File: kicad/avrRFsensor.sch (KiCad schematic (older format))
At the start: 13 parts, among them U1 ATTINY85-20SU, X1 18MHz HC49USSMD

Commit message: schematics on atmega168 tqfp32
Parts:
- removed U1: ATTINY85-20SU, SO8-200, symbol ATTINY85-S
- added D3: 3V6, symbol ZENER
- added R5: 25, symbol R
- added R6, R7, R8: 10k, symbol R
- added U1: ATMEGA168PA-A, TQFP32, symbol ATMEGA168PA-A
- added U2: RFM69, ~, symbol RFM69
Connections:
- net labels added: MISO_RFM, MISO_USB, MOSI_RFM, SCK_RFM, SCK_USB, VCC +5
- wire segments 36 -> 56
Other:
- moved on the sheet: C3
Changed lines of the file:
@@
 LIBS:contrib
 LIBS:valves
+LIBS:rfm69
 LIBS:avrRFsensor-cache
 EELAYER 27 0
@@
 Connection ~ 1500 2150
 Wire Wire Line
-	3400 2750 3850 2750
-Wire Wire Line
 	1500 1350 1500 1450
-Connection ~ 6700 3250
-Wire Wire Line
-	3400 2850 3850 2850
+Connection ~ 1050 7300
 Wire Wire Line
 	950  4650 1100 4650
@@
 L GND #PWR01
 U 1 1 4E041C8A
-P 6700 3300
-F 0 "#PWR01" H 6700 3300 30  0001 C CNN
-F 1 "GND" H 6700 3230 30  0001 C CNN
-F 2 "" H 6700 3300 60  0001 C CNN
-F 3 "" H 6700 3300 60  0001 C CNN
-	1    6700 3300
+P 1050 7350
+F 0 "#PWR01" H 1050 7350 30  0001 C CNN
+F 1 "GND" H 1050 7280 30  0001 C CNN
+F 2 "" H 1050 7350 60  0001 C CNN
+F 3 "" H 1050 7350 60  0001 C CNN
+	1    1050 7350
 	1    0    0    -1
 $EndComp
@@
 	1    1350 1000
 	0    1    1    0
-$EndComp
-$Comp
-L ATTINY85-S U1
-U 1 1 4E03B504
-P 5200 3000
-F 0 "U1" H 5300 3050 60  0000 C CNN
-F 1 "ATTINY85-20SU" H 5700 2750 60  0000 C CNN
-F 2 "SO8-200" H 5450 2250 60  0001 C CNN
-F 3 "" H 5200 3000 60  0001 C CNN
-	1    5200 3000
-	1    0    0    -1
 $EndComp
 $Comp
@@
 L CP1 C3
 U 1 1 4B61D8DC
-P 6700 3000
-F 0 "C3" H 6750 3100 50  0000 L CNN
-F 1 "4.7uF" H 6750 2900 50  0000 L CNN
-F 2 "" H 6700 3000 60  0001 C CNN
-F 3 "" H 6700 3000 60  0001 C CNN
-	1    6700 3000
+P 1050 7050
+F 0 "C3" H 1100 7150 50  0000 L CNN
+F 1 "4.7uF" H 1100 6950 50  0000 L CNN
+F 2 "" H 1050 7050 60  0001 C CNN
+F 3 "" H 1050 7050 60  0001 C CNN
+	1    1050 7050
 	1    0    0    -1
 $EndComp
@@
 	1    0    0    -1
 $EndComp
-Text GLabel 6900 2750 2    60   Input ~ 0
+Text GLabel 1250 6800 2    60   Input ~ 0
 VCC
 Text GLabel 1600 4350 2    60   Input ~ 0
@@
 Wire Wire Line
 	1000 1000 1100 1000
-Text GLabel 6900 3250 2    60   Input ~ 0
+Text GLabel 1250 7300 2    60   Input ~ 0
 GND
 Text GLabel 900  1350 0    60   Input ~ 0
@@
 Wire Wire Line
 	900  1350 1000 1350
-Text GLabel 3400 3050 0    60   Input ~ 0
+Text GLabel 5500 2900 2    60   Input ~ 0
 XTAL1
-Text GLabel 3400 3150 0    60   Input ~ 0
+Text GLabel 5500 3000 2    60   Input ~ 0
 XTAL2
-Wire Wire Line
-	3400 3050 3850 3050
-Wire Wire Line
-	3850 3150 3400 3150
 Text GLabel 950  5000 0    60   Input ~ 0
 GND
-Text GLabel 3400 3250 0    60   Input ~ 0
+Text GLabel 5500 3750 2    60   Input ~ 0
 RESET
-Wire Wire Line
-	3850 3250 3400 3250
 Text GLabel 1300 2900 2    60   Input ~ 0
 MOSI
 Wire Wire Line
 	1300 2900 1150 2900
-Text GLabel 3400 2750 0    60   Input ~ 0
+Text GLabel 5500 2600 2    60   Input ~ 0
 MOSI
 Wire Wire Line
-	6700 3200 6700 3300
-Wire Wire Line
-	6700 2700 6700 2800
-Connection ~ 6700 2750
+	1050 7250 1050 7350
+Wire Wire Line
+	1050 6750 1050 6850
+Connection ~ 1050 6800
 $Comp
 L VCC #PWR02
 U 1 1 54B791F6
-P 6700 2700
-F 0 "#PWR02" H 6700 2800 30  0001 C CNN
-F 1 "VCC" H 6700 2800 30  0000 C CNN
-F 2 "" H 6700 2700 60  0000 C CNN
-F 3 "" H 6700 2700 60  0000 C CNN
-	1    6700 2700
-	1    0    0    -1
-$EndComp
-Wire Wire Line
-	6550 3250 6900 3250
-Wire Wire Line
-	6550 2750 6900 2750
+P 1050 6750
+F 0 "#PWR02" H 1050 6850 30  0001 C CNN
+F 1 "VCC" H 1050 6850 30  0000 C CNN
+F 2 "" H 1050 6750 60  0000 C CNN
+F 3 "" H 1050 6750 60  0000 C CNN
+	1    1050 6750
+	1    0    0    -1
+$EndComp
 Text GLabel 1300 2800 2    60   Input ~ 0
 MISO
 Wire Wire Line
 	1300 2800 1150 2800
-Text GLabel 3400 2850 0    60   Input ~ 0
+Text GLabel 5500 2700 2    60   Input ~ 0
 MISO
 Text GLabel 1600 4100 2    60   Input ~ 0
-MISO
+MISO_USB
 Wire Wire Line
 	1500 4100 1600 4100
@@
 Wire Wire Line
 	1300 2700 1150 2700
-Text GLabel 3400 2950 0    60   Input ~ 0
+Text GLabel 5500 2800 2    60   Input ~ 0
 SCK
-Wire Wire Line
-	3850 2950 3400 2950
 Text GLabel 1600 3850 2    60   Input ~ 0
-SCK
+SCK_USB
 Wire Wire Line
 	1500 3850 1600 3850
 Text GLabel 1450 5600 2    60   Input ~ 0
-VCC
+VCC +5
 Text GLabel 1450 5300 2    60   Input ~ 0
 GND
@@
 Wire Wire Line
 	1000 4350 900  4350
+$Comp
+L ATMEGA168PA-A U1
+U 1 1 54B7A49D
+P 4300 3400
+F 0 "U1" H 3550 4650 40  0000 L BNN
+F 1 "ATMEGA168PA-A" H 4700 2000 40  0000 L BNN
+F 2 "TQFP32" H 4300 3400 30  0000 C CIN
+F 3 "" H 4300 3400 60  0000 C CNN
+	1    4300 3400
+	1    0    0    -1
+$EndComp
+Wire Wire Line
+	5300 3750 5500 3750
+Wire Wire Line
+	5500 3000 5300 3000
+Wire Wire Line
+	5500 2900 5300 2900
+Wire Wire Line
+	1250 7300 1050 7300
+Wire Wire Line
+	1250 6800 1050 6800
+Text GLabel 3200 4600 0    60   Input ~ 0
+GND
+Text GLabel 3200 2300 0    60   Input ~ 0
+VCC
+Text GLabel 3200 2400 0    60   Input ~ 0
+VCC
+Wire Wire Line
+	3400 2300 3200 2300
+Wire Wire Line
+	3200 2400 3400 2400
+Text GLabel 3200 2600 0    60   Input ~ 0
+VCC
+Wire Wire Line
+	3400 2600 3200 2600
+Wire Wire Line
+	5500 2700 5300 2700
+Wire Wire Line
+	5500 2800 5300 2800
+Wire Wire Line
+	5500 2600 5300 2600
+Wire Wire Line
+	3400 4600 3200 4600
+Text GLabel 3200 4500 0    60   Input ~ 0
+GND
+Text GLabel 3200 4400 0    60   Input ~ 0
+GND
+Wire Wire Line
+	3200 4400 3400 4400
+Wire Wire Line
+	3400 4500 3200 4500
+$Comp
+L RFM69 U2
+U 1 1 54B7BF4D
+P 3950 5650
+F 0 "U2" H 4000 5750 60  0000 C CNN
+F 1 "RFM69" H 4200 4800 60  0000 C CNN
+F 2 "~" H 3950 5700 60  0000 C CNN
+F 3 "~" H 3950 5700 60  0000 C CNN
+	1    3950 5650
+	1    0    0    -1
+$EndComp
+Text GLabel 4900 6150 2    60   Input ~ 0
+GND
+Text GLabel 4900 6350 2    60   Input ~ 0
+GND
+Text GLabel 4900 5750 2    60   Input ~ 0
+GND
+Wire Wire Line
+	4900 5750 4750 5750
+Wire Wire Line
+	4750 6150 4900 6150
+Wire Wire Line
+	4900 6350 4750 6350
+Text GLabel 3500 6350 0    60   Input ~ 0
+VCC
+Wire Wire Line
+	3500 6350 3650 6350
+Text GLabel 5750 6050 2    60   Input ~ 0
+SCK_RFM
+Text GLabel 5750 5950 2    60   Input ~ 0
+MISO_RFM
+Text GLabel 5750 5850 2    60   Input ~ 0
+MOSI_RFM
+Wire Wire Line
+	4750 5850 5100 5850
+Wire Wire Line
+	4750 5950 5100 5950
+Wire Wire Line
+	4750 6050 5100 6050
+$Comp
+L R R6
+U 1 1 54B7CD7C
+P 5350 5850
+F 0 "R6" V 5350 5750 50  0000 C CNN
+F 1 "10k" V 5350 5900 50  0000 C CNN
+F 2 "" H 5350 5850 60  0001 C CNN
+F 3 "" H 5350 5850 60  0001 C CNN
+	1    5350 5850
+	0    1    1    0
+$EndComp
+$Comp
+L R R7
+U 1 1 54B7CDBD
+P 5350 5950
+F 0 "R7" V 5350 5850 50  0000 C CNN
+F 1 "10k" V 5350 6000 50  0000 C CNN
+F 2 "" H 5350 5950 60  0001 C CNN
+F 3 "" H 5350 5950 60  0001 C CNN
+	1    5350 5950
+	0    1    1    0
+$EndComp
+$Comp
+L R R8
+U 1 1 54B7CDC3
+P 5350 6050
+F 0 "R8" V 5350 5950 50  0000 C CNN
+F 1 "10k" V 5350 6100 50  0000 C CNN
+F 2 "" H 5350 6050 60  0001 C CNN
+F 3 "" H 5350 6050 60  0001 C CNN
+	1    5350 6050
+	0    1    1    0
+$EndComp
+Wire Wire Line
+	5600 6050 5750 6050
+Wire Wire Line
+	5750 5950 5600 5950
+Wire Wire Line
+	5600 5850 5750 5850
+Text GLabel 1050 6000 0    60   Input ~ 0
+VCC +5
+$Comp
+L R R5
+U 1 1 54B7D03F
+P 1400 6000
+F 0 "R5" V 1400 5900 50  0000 C CNN
+F 1 "25" V 1400 6050 50  0000 C CNN
+F 2 "" H 1400 6000 60  0001 C CNN
+F 3 "" H 1400 6000 60  0001 C CNN
+	1    1400 6000
+	0    1    1    0
+$EndComp
+$Comp
+L ZENER D3
+U 1 1 54B7D045
+P 1750 6300
+F 0 "D3" H 1750 6400 50  0000 C CNN
+F 1 "3V6" H 1750 6200 40  0000 C CNN
+F 2 "" H 1750 6300 60  0001 C CNN
+F 3 "" H 1750 6300 60  0001 C CNN
+	1    1750 6300
+	0    -1   -1   0
+$EndComp
+Text GLabel 1850 6000 2    60   Input ~ 0
+VCC
+Wire Wire Line
+	1050 6000 1150 6000
+Wire Wire Line
+	1650 6000 1850 6000
+Wire Wire Line
+	1750 6100 1750 6000
+Connection ~ 1750 6000
+Text GLabel 1850 6500 2    60   Input ~ 0
+GND
+Wire Wire Line
+	1750 6500 1850 6500
 $EndSCHEMATC

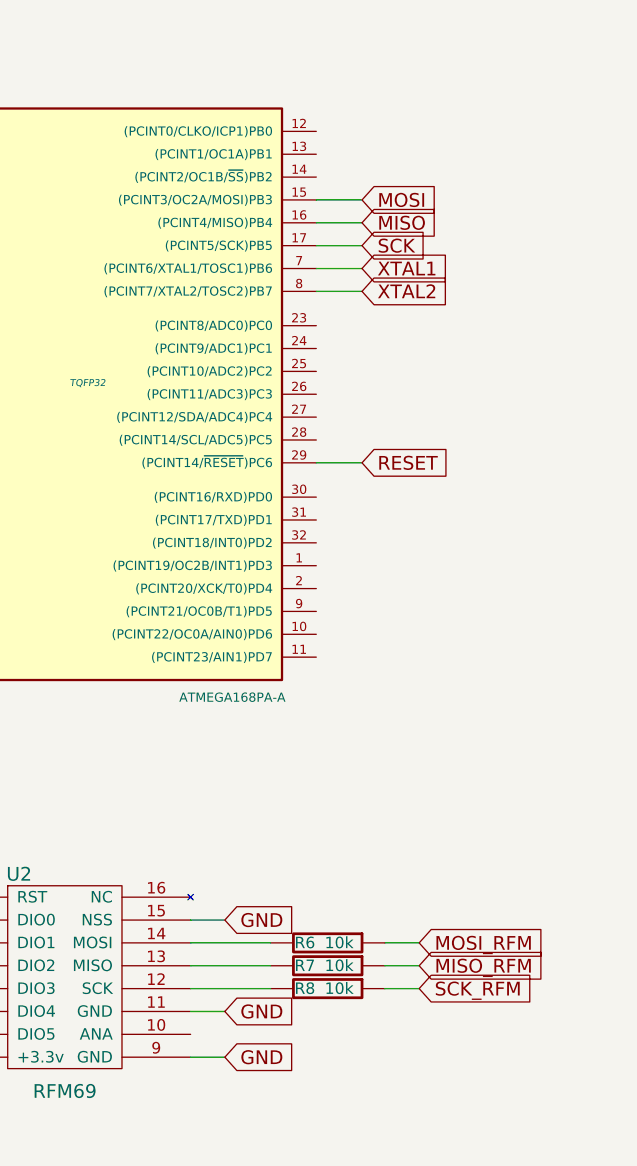
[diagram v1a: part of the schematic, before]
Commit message: Remade pcb for atmega168pa-au microcontroller. will see results.
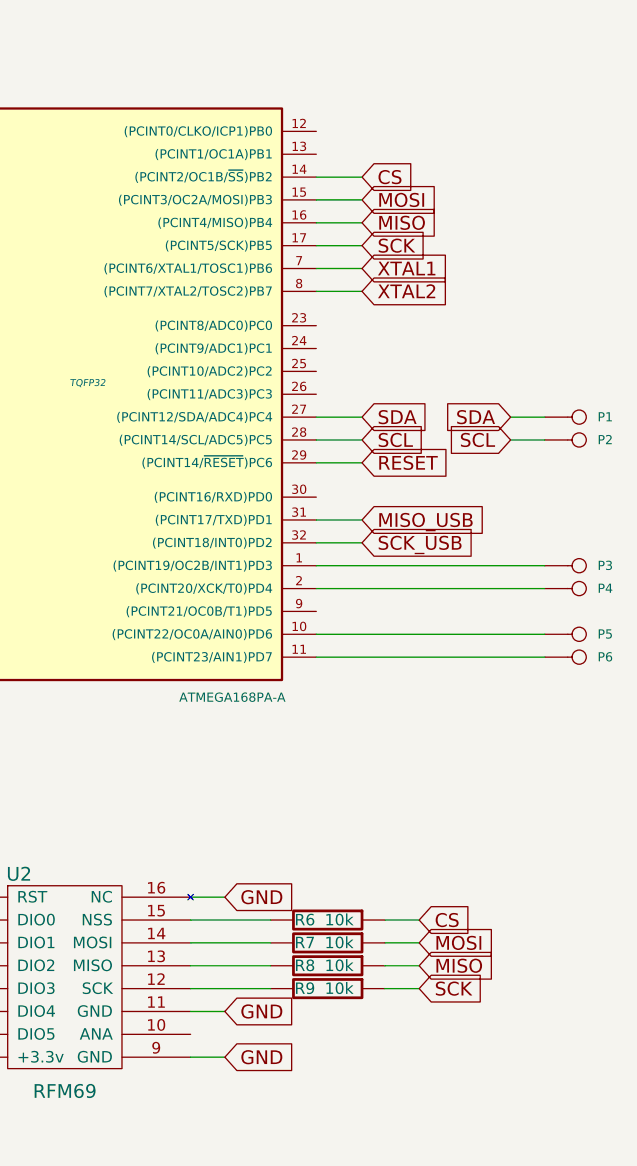
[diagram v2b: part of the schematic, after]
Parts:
- added P1, P2, P3, P4, P5, P6: CONN_1, symbol CONN_1
- added R6: 10k, symbol R
- renumbered R6 to R7, R7 to R8, R8 to R9
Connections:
- net MISO_RFM is gone; now on net MISO: R8.1
- net MOSI_RFM is gone; now on net MOSI: R7.1
- net SCK_RFM is gone; now on net SCK: R9.1
- net GND: now also U2.16 (NC); no longer U2.15 (NSS)
- net MISO_USB: now also U1.31 ((PCINT17/TXD)PD1)
- net SCK_USB: now also U1.32 ((PCINT18/INT0)PD2)
- net at U1.1 ((PCINT19/OC2B/INT1)PD3): now also P3.1
- net at U1.10 ((PCINT22/OC0A/AIN0)PD6): now also P5.1
- net at U1.11 ((PCINT23/AIN1)PD7): now also P6.1
- net CS: now reaches U1.14 ((PCINT2/OC1B/~SS~)PB2)
- net CS: now also R6.1
- net at U1.2 ((PCINT20/XCK/T0)PD4): now also P4.1
- net SDA: now reaches U1.27 ((PCINT12/SDA/ADC4)PC4)
- net SDA: now also P1.1
- net SCL: now reaches U1.28 ((PCINT14/SCL/ADC5)PC5)
- net SCL: now also P2.1
- new net: R6.2, U2.15 (NSS)
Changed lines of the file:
@@
 Sheet 1 1
 Title ""
-Date "15 jan 2015"
+Date "17 jan 2015"
 Rev ""
 Comp ""
@@
 Text GLabel 4900 6350 2    60   Input ~ 0
 GND
-Text GLabel 4900 5750 2    60   Input ~ 0
-GND
-Wire Wire Line
-	4900 5750 4750 5750
+Text GLabel 5750 5750 2    60   Input ~ 0
+CS
 Wire Wire Line
 	4750 6150 4900 6150
@@
 	3500 6350 3650 6350
 Text GLabel 5750 6050 2    60   Input ~ 0
-SCK_RFM
+SCK
 Text GLabel 5750 5950 2    60   Input ~ 0
-MISO_RFM
+MISO
 Text GLabel 5750 5850 2    60   Input ~ 0
-MOSI_RFM
+MOSI
 Wire Wire Line
 	4750 5850 5100 5850
@@
 	4750 6050 5100 6050
 $Comp
-L R R6
+L R R7
 U 1 1 54B7CD7C
 P 5350 5850
-F 0 "R6" V 5350 5750 50  0000 C CNN
+F 0 "R7" V 5350 5750 50  0000 C CNN
 F 1 "10k" V 5350 5900 50  0000 C CNN
 F 2 "" H 5350 5850 60  0001 C CNN
@@
 $EndComp
 $Comp
-L R R7
+L R R8
 U 1 1 54B7CDBD
 P 5350 5950
-F 0 "R7" V 5350 5850 50  0000 C CNN
+F 0 "R8" V 5350 5850 50  0000 C CNN
 F 1 "10k" V 5350 6000 50  0000 C CNN
 F 2 "" H 5350 5950 60  0001 C CNN
@@
 $EndComp
 $Comp
-L R R8
+L R R9
 U 1 1 54B7CDC3
 P 5350 6050
-F 0 "R8" V 5350 5950 50  0000 C CNN
+F 0 "R9" V 5350 5950 50  0000 C CNN
 F 1 "10k" V 5350 6100 50  0000 C CNN
 F 2 "" H 5350 6050 60  0001 C CNN
@@
 Wire Wire Line
 	1750 6500 1850 6500
+$Comp
+L R R6
+U 1 1 54BA358D
+P 5350 5750
+F 0 "R6" V 5350 5650 50  0000 C CNN
+F 1 "10k" V 5350 5800 50  0000 C CNN
+F 2 "" H 5350 5750 60  0001 C CNN
+F 3 "" H 5350 5750 60  0001 C CNN
+	1    5350 5750
+	0    1    1    0
+$EndComp
+Wire Wire Line
+	4750 5750 5100 5750
+Wire Wire Line
+	5750 5750 5600 5750
+Text GLabel 4900 5650 2    60   Input ~ 0
+GND
+Wire Wire Line
+	4750 5650 4900 5650
+Text GLabel 5500 2500 2    60   Input ~ 0
+CS
+Wire Wire Line
+	5500 2500 5300 2500
+Text GLabel 5500 3550 2    60   Input ~ 0
+SDA
+Text GLabel 5500 3650 2    60   Input ~ 0
+SCL
+Wire Wire Line
+	5500 3550 5300 3550
+Wire Wire Line
+	5300 3650 5500 3650
+Text GLabel 5500 4100 2    60   Input ~ 0
+SCK_USB
+Text GLabel 5500 4000 2    60   Input ~ 0
+MISO_USB
+Wire Wire Line
+	5500 4100 5300 4100
+Wire Wire Line
+	5500 4000 5300 4000
+$Comp
+L CONN_1 P1
+U 1 1 54BA8548
+P 6450 3550
+F 0 "P1" H 6530 3550 40  0000 L CNN
+F 1 "CONN_1" H 6450 3605 30  0001 C CNN
+F 2 "" H 6450 3550 60  0000 C CNN
+F 3 "" H 6450 3550 60  0000 C CNN
+	1    6450 3550
+	1    0    0    -1
+$EndComp
+$Comp
+L CONN_1 P2
+U 1 1 54BA8557
+P 6450 3650
+F 0 "P2" H 6530 3650 40  0000 L CNN
+F 1 "CONN_1" H 6450 3705 30  0001 C CNN
+F 2 "" H 6450 3650 60  0000 C CNN
+F 3 "" H 6450 3650 60  0000 C CNN
+	1    6450 3650
+	1    0    0    -1
+$EndComp
+Text GLabel 6150 3550 0    60   Input ~ 0
+SDA
+Text GLabel 6150 3650 0    60   Input ~ 0
+SCL
+Wire Wire Line
+	6150 3550 6300 3550
+Wire Wire Line
+	6150 3650 6300 3650
+$Comp
+L CONN_1 P3
+U 1 1 54BA86B7
+P 6450 4200
+F 0 "P3" H 6530 4200 40  0000 L CNN
+F 1 "CONN_1" H 6450 4255 30  0001 C CNN
+F 2 "" H 6450 4200 60  0000 C CNN
+F 3 "" H 6450 4200 60  0000 C CNN
+	1    6450 4200
+	1    0    0    -1
+$EndComp
+$Comp
+L CONN_1 P4
+U 1 1 54BA86BD
+P 6450 4300
+F 0 "P4" H 6530 4300 40  0000 L CNN
+F 1 "CONN_1" H 6450 4355 30  0001 C CNN
+F 2 "" H 6450 4300 60  0000 C CNN
+F 3 "" H 6450 4300 60  0000 C CNN
+	1    6450 4300
+	1    0    0    -1
+$EndComp
+Wire Wire Line
+	5300 4200 6300 4200
+Wire Wire Line
+	5300 4300 6300 4300
+$Comp
+L CONN_1 P5
+U 1 1 54BA884D
+P 6450 4500
+F 0 "P5" H 6530 4500 40  0000 L CNN
+F 1 "CONN_1" H 6450 4555 30  0001 C CNN
+F 2 "" H 6450 4500 60  0000 C CNN
+F 3 "" H 6450 4500 60  0000 C CNN
+	1    6450 4500
+	1    0    0    -1
+$EndComp
+Wire Wire Line
+	6300 4500 5300 4500
+$Comp
+L CONN_1 P6
+U 1 1 54BA88D5
+P 6450 4600
+F 0 "P6" H 6530 4600 40  0000 L CNN
+F 1 "CONN_1" H 6450 4655 30  0001 C CNN
+F 2 "" H 6450 4600 60  0000 C CNN
+F 3 "" H 6450 4600 60  0000 C CNN
+	1    6450 4600
+	1    0    0    -1
+$EndComp
+Wire Wire Line
+	6300 4600 5300 4600
 $EndSCHEMATC

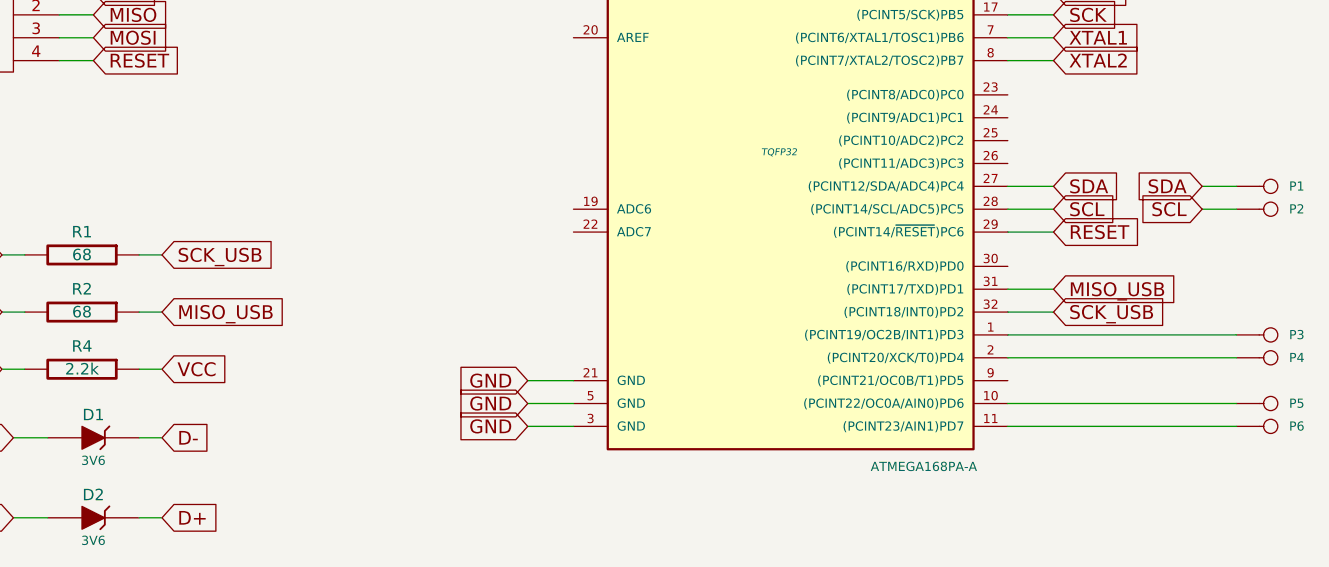
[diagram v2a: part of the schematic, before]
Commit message: not working. just started transformation on mega168. pcb is ok i think. will see
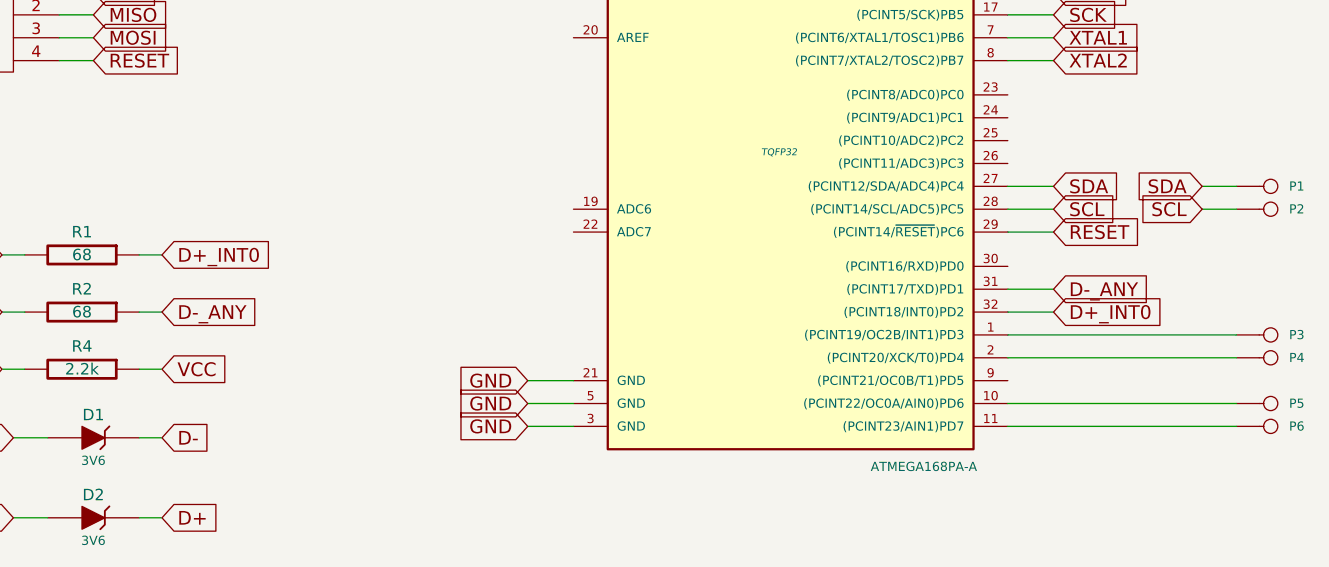
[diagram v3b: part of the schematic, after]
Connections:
- net MISO_USB renamed D-_ANY
- net SCK_USB renamed D+_INT0
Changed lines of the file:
@@
 Sheet 1 1
 Title ""
-Date "17 jan 2015"
+Date "21 jan 2015"
 Rev ""
 Comp ""
@@
 MISO
 Text GLabel 1600 4100 2    60   Input ~ 0
-MISO_USB
+D-_ANY
 Wire Wire Line
 	1500 4100 1600 4100
@@
 SCK
 Text GLabel 1600 3850 2    60   Input ~ 0
-SCK_USB
+D+_INT0
 Wire Wire Line
 	1500 3850 1600 3850
@@
 	5300 3650 5500 3650
 Text GLabel 5500 4100 2    60   Input ~ 0
-SCK_USB
+D+_INT0
 Text GLabel 5500 4000 2    60   Input ~ 0
-MISO_USB
+D-_ANY
 Wire Wire Line
 	5500 4100 5300 4100

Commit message: timestamp unsigned long = very huge number. Some additional sturctures
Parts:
- R5: value 25 -> 24
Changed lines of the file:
@@
 Sheet 1 1
 Title ""
-Date "21 jan 2015"
+Date "23 jan 2015"
 Rev ""
 Comp ""
@@
 P 1400 6000
 F 0 "R5" V 1400 5900 50  0000 C CNN
-F 1 "25" V 1400 6050 50  0000 C CNN
+F 1 "24" V 1400 6050 50  0000 C CNN
 F 2 "" H 1400 6000 60  0001 C CNN
 F 3 "" H 1400 6000 60  0001 C CNN

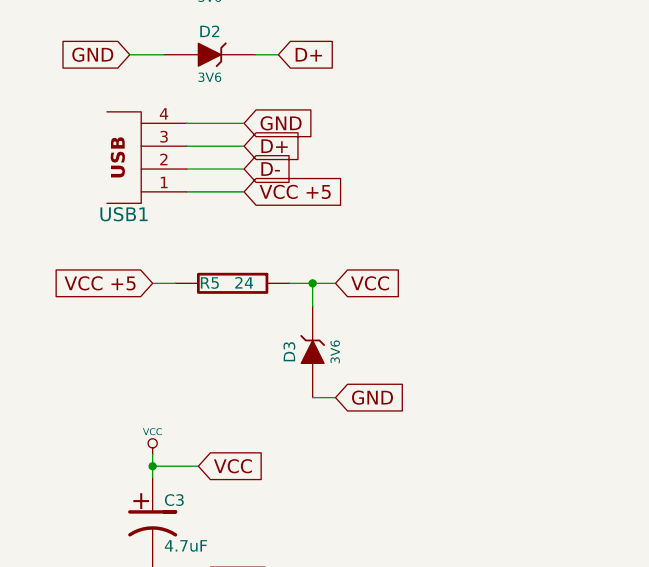
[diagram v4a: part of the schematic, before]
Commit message: changed stabilizer nominals in Kicad, Moved to atmega168p processor. Started testing
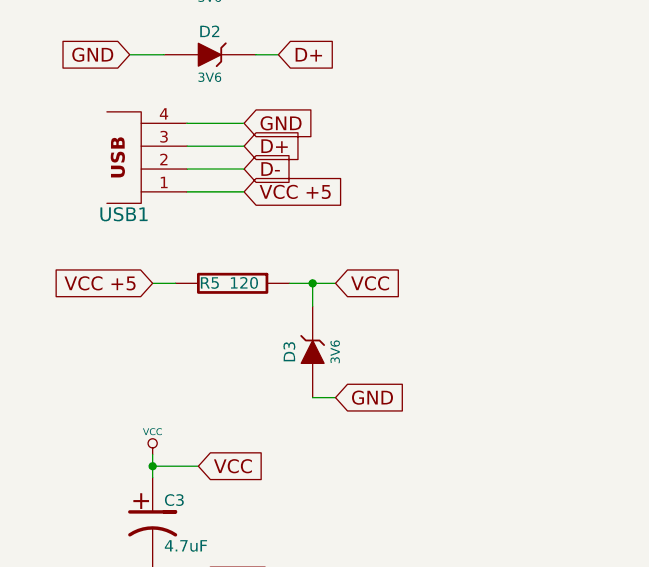
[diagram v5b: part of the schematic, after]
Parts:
- R5: value 24 -> 120
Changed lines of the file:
@@
 Sheet 1 1
 Title ""
-Date "23 jan 2015"
+Date "26 jan 2015"
 Rev ""
 Comp ""
@@
 P 1400 6000
 F 0 "R5" V 1400 5900 50  0000 C CNN
-F 1 "24" V 1400 6050 50  0000 C CNN
+F 1 "120" V 1400 6050 50  0000 C CNN
 F 2 "" H 1400 6000 60  0001 C CNN
 F 3 "" H 1400 6000 60  0001 C CNN
